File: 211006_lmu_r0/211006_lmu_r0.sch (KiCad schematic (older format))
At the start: 4 parts

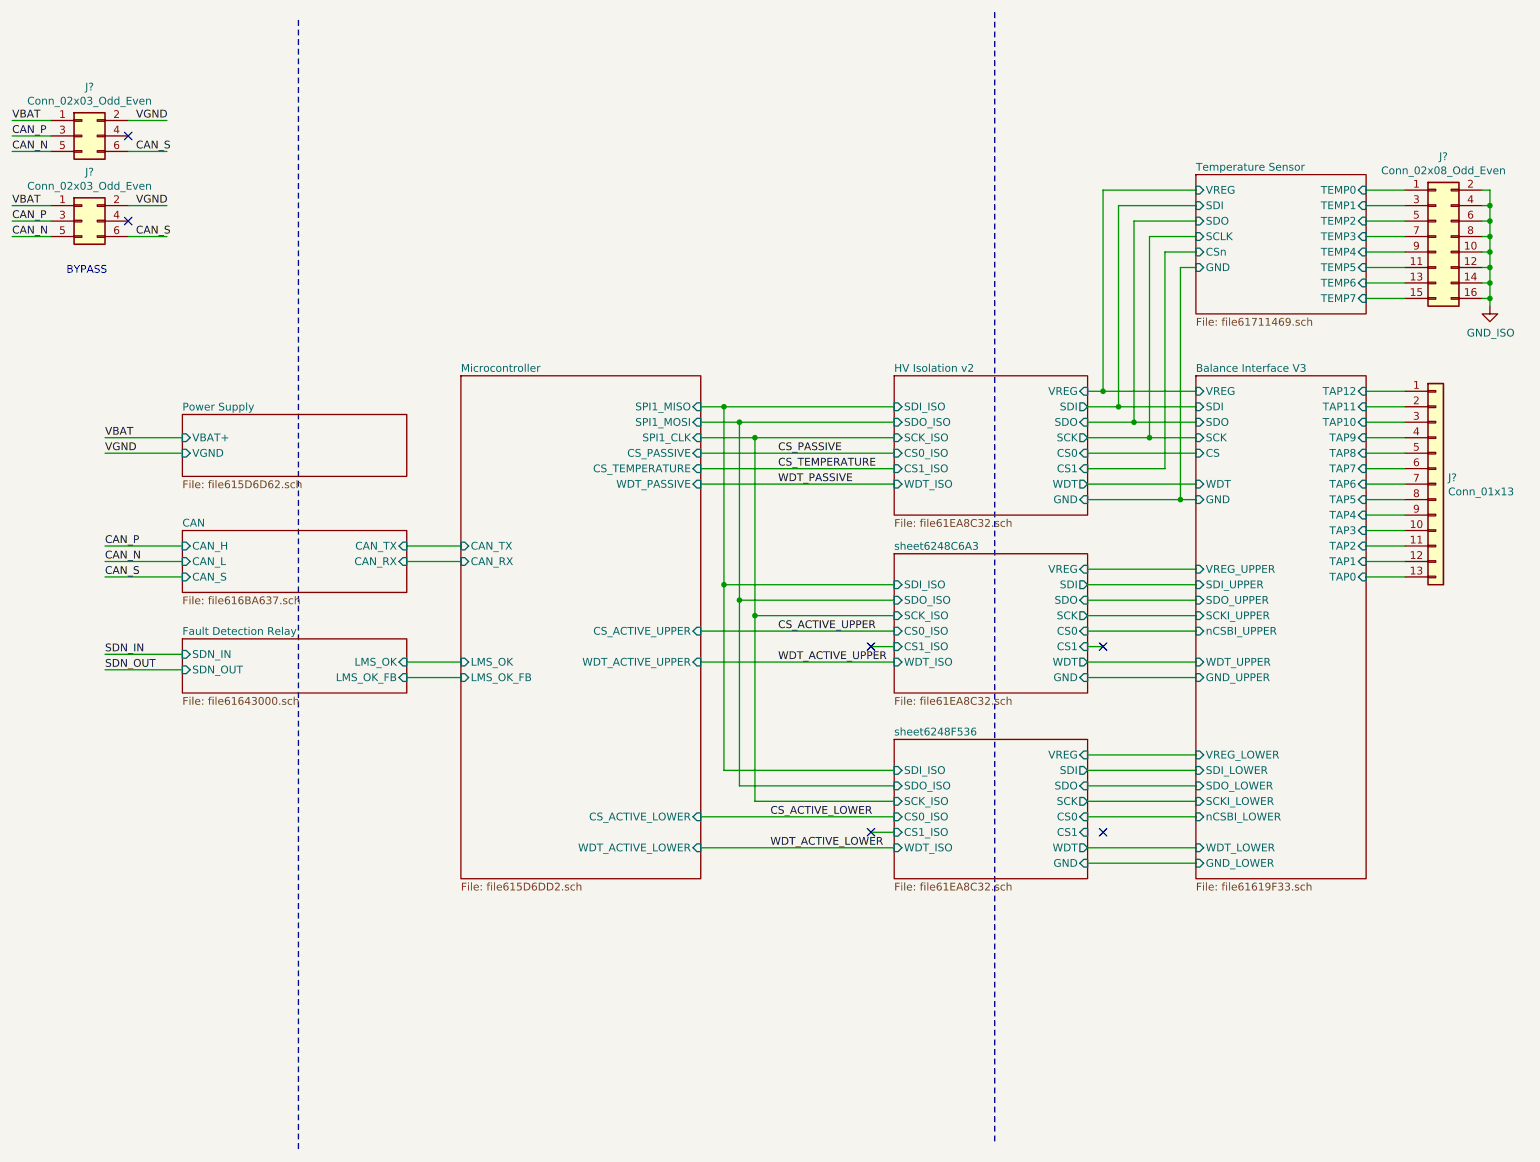
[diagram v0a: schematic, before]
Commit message: Updated BOM and footprints for non-hv components
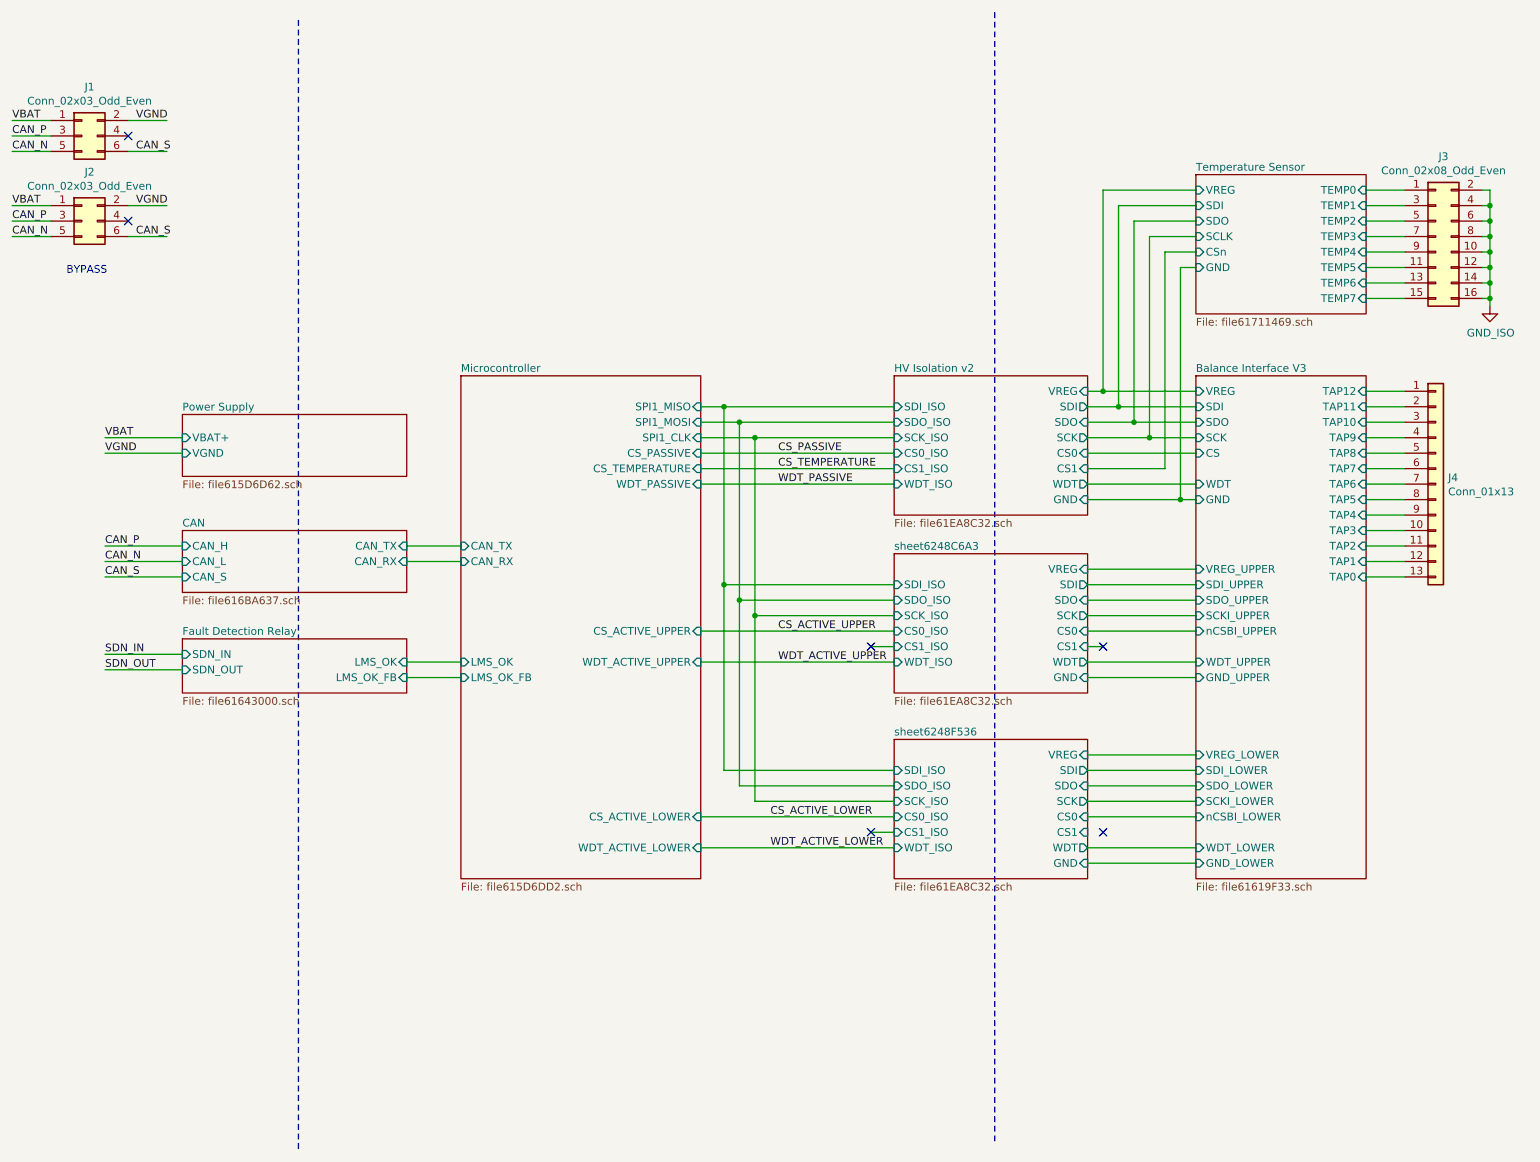
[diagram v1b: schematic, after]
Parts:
- gave numbers to parts that had none: 4
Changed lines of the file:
@@
 	1950 3250 2450 3250
 $Comp
-L Connector_Generic:Conn_02x03_Odd_Even J?
+L Connector_Generic:Conn_02x03_Odd_Even J1
 U 1 1 616F9826
 P 1800 1200
-F 0 "J?" H 1850 1517 50  0000 C CNN
+F 0 "J1" H 1850 1517 50  0000 C CNN
 F 1 "Conn_02x03_Odd_Even" H 1850 1426 50  0000 C CNN
 F 2 "" H 1800 1200 50  0001 C CNN
@@
 	1600 1300 1350 1300
 $Comp
-L Connector_Generic:Conn_02x03_Odd_Even J?
+L Connector_Generic:Conn_02x03_Odd_Even J2
 U 1 1 6170BFBA
 P 1800 1750
-F 0 "J?" H 1850 2067 50  0000 C CNN
+F 0 "J2" H 1850 2067 50  0000 C CNN
 F 1 "Conn_02x03_Odd_Even" H 1850 1976 50  0000 C CNN
 F 2 "" H 1800 1750 50  0001 C CNN
@@
 $EndSheet
 $Comp
-L Connector_Generic:Conn_01x13 J?
+L Connector_Generic:Conn_01x13 J4
 U 1 1 616A746A
 P 10550 3450
-F 0 "J?" H 10630 3492 50  0000 L CNN
+F 0 "J4" H 10630 3492 50  0000 L CNN
 F 1 "Conn_01x13" H 10630 3401 50  0000 L CNN
 F 2 "" H 10550 3450 50  0001 C CNN
@@
 	7700 400  7700 7700
 $Comp
-L Connector_Generic:Conn_02x08_Odd_Even J?
+L Connector_Generic:Conn_02x08_Odd_Even J3
 U 1 1 6170F017
 P 10550 1850
-F 0 "J?" H 10600 2367 50  0000 C CNN
+F 0 "J3" H 10600 2367 50  0000 C CNN
 F 1 "Conn_02x08_Odd_Even" H 10600 2276 50  0000 C CNN
 F 2 "" H 10550 1850 50  0001 C CNN
@@
 	3900 4600 4250 4600
 $Comp
-L gnd_iso:GND_ISO #PWR?
+L gnd_iso:GND_ISO #PWR0101
 U 1 1 61694729
 P 10900 2300
-F 0 "#PWR?" H 10900 2050 50  0001 C CNN
+F 0 "#PWR0101" H 10900 2050 50  0001 C CNN
 F 1 "GND_ISO" H 10905 2127 50  0000 C CNN
 F 2 "" H 10900 2300 50  0001 C CNN

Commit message: Cleaned up last components missing footprint refs
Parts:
- J1, J2: footprint (none) -> Connector_Molex:Molex_Mini-Fit_Jr_5566-06A_2x03_P4.20mm_Vertical
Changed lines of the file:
@@
 F 0 "J1" H 1850 1517 50  0000 C CNN
 F 1 "Conn_02x03_Odd_Even" H 1850 1426 50  0000 C CNN
-F 2 "" H 1800 1200 50  0001 C CNN
+F 2 "Connector_Molex:Molex_Mini-Fit_Jr_5566-06A_2x03_P4.20mm_Vertical" H 1800 1200 50  0001 C CNN
 F 3 "~" H 1800 1200 50  0001 C CNN
 	1    1800 1200
@@
 F 0 "J2" H 1850 2067 50  0000 C CNN
 F 1 "Conn_02x03_Odd_Even" H 1850 1976 50  0000 C CNN
-F 2 "" H 1800 1750 50  0001 C CNN
+F 2 "Connector_Molex:Molex_Mini-Fit_Jr_5566-06A_2x03_P4.20mm_Vertical" H 1800 1750 50  0001 C CNN
 F 3 "~" H 1800 1750 50  0001 C CNN
 	1    1800 1750

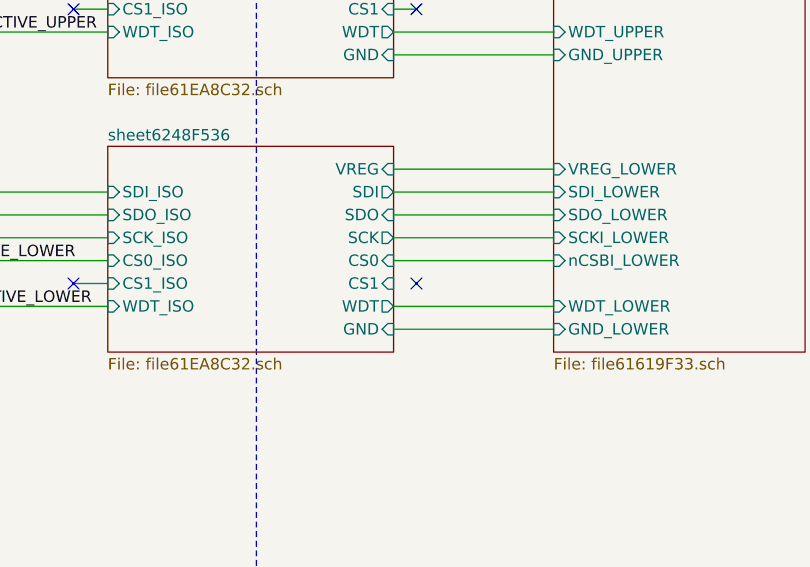
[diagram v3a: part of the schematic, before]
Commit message: Updated with Mouser links for BOM
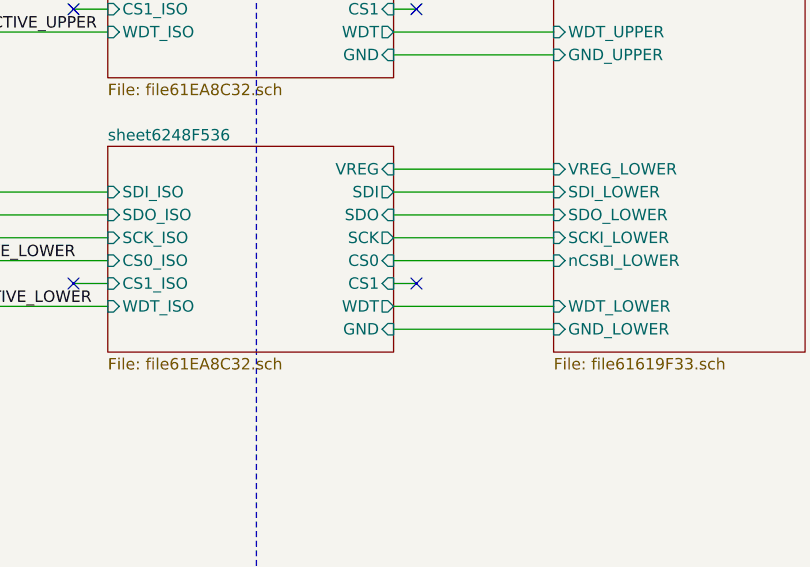
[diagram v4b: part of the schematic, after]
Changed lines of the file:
@@
 F15 "LMS_OK_FB" I L 4250 4700 50
 $EndSheet
+Wire Wire Line
+	8400 5700 8300 5700
 $EndSCHEMATC
